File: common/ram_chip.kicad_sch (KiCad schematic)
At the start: 3 parts, among them U8 71016S12PHG8

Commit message: Memory Controller- Initial setup
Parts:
- renumbered C9 to C17, C10 to C18, U8 to U14

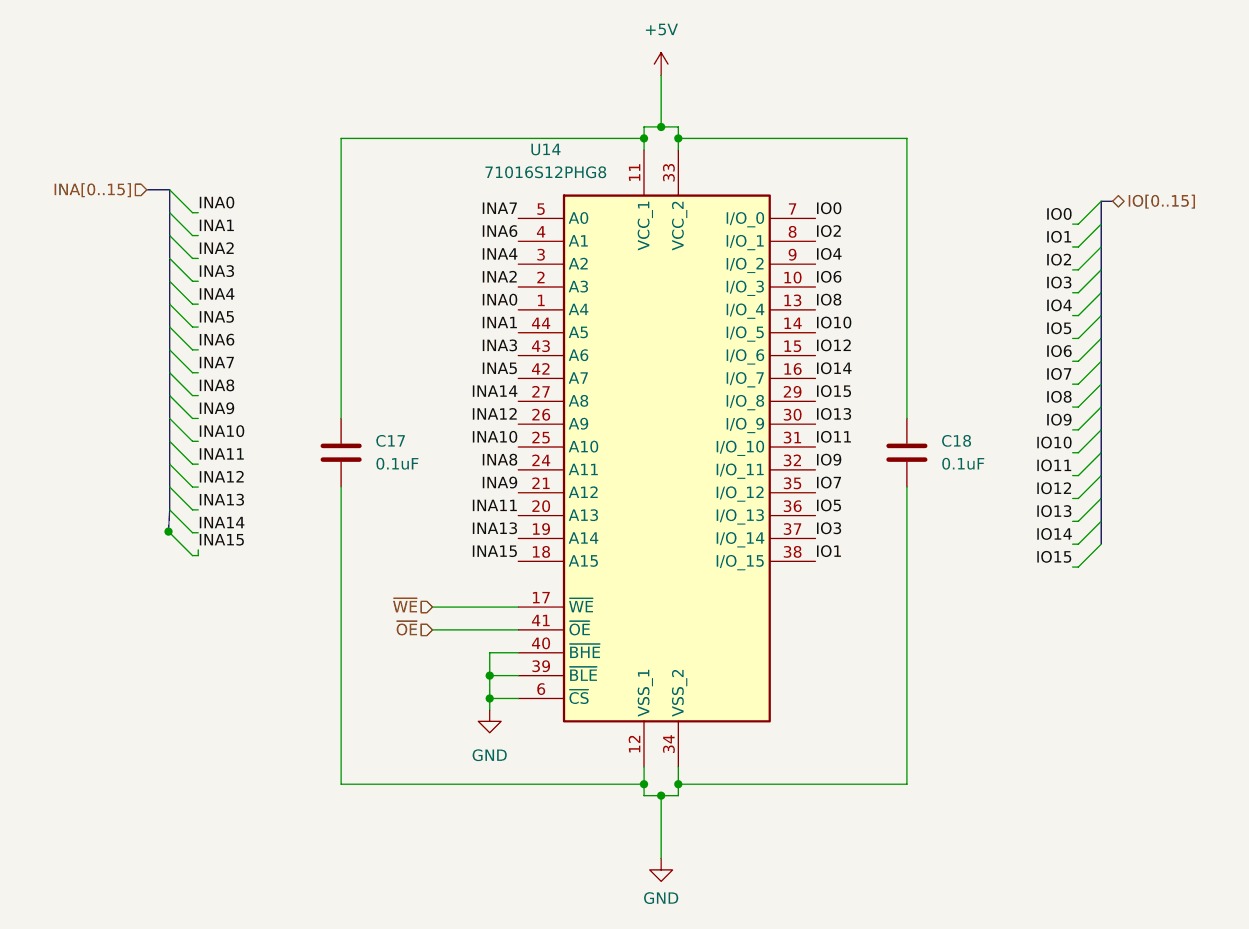
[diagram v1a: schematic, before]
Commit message: Memory Controller fabrication checks complete
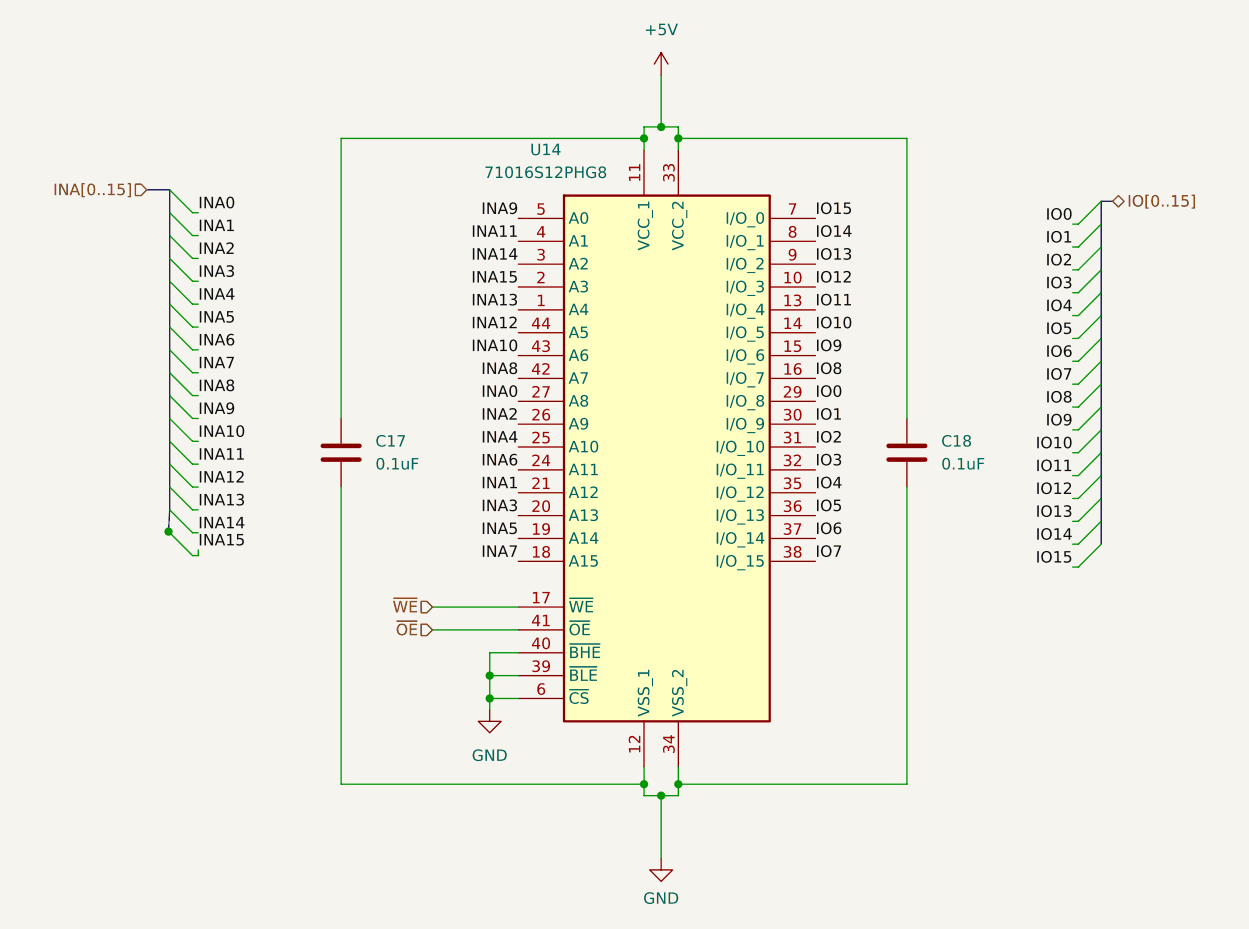
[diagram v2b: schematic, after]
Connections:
- net INA0: now also U14.27 (A8); no longer U14.1 (A4)
- net INA1: now also U14.21 (A12); no longer U14.44 (A5)
- net INA10: now also U14.43 (A6); no longer U14.25 (A10)
- net INA11: now also U14.4 (A1); no longer U14.20 (A13)
- net INA12: now also U14.44 (A5); no longer U14.26 (A9)
- net INA13: now also U14.1 (A4); no longer U14.19 (A14)
- net INA14: now also U14.3 (A2); no longer U14.27 (A8)
- net INA15: now also U14.2 (A3); no longer U14.18 (A15)
- net INA2: now also U14.26 (A9); no longer U14.2 (A3)
- net INA3: now also U14.20 (A13); no longer U14.43 (A6)
- net INA4: now also U14.25 (A10); no longer U14.3 (A2)
- net INA5: now also U14.19 (A14); no longer U14.42 (A7)
- net INA6: now also U14.24 (A11); no longer U14.4 (A1)
- net INA7: now also U14.18 (A15); no longer U14.5 (A0)
- net INA8: now also U14.42 (A7); no longer U14.24 (A11)
- net INA9: now also U14.5 (A0); no longer U14.21 (A12)
- net IO0: now also U14.29 (I/O_8); no longer U14.7 (I/O_0)
- net IO1: now also U14.30 (I/O_9); no longer U14.38 (I/O_15)
- net IO11: now also U14.13 (I/O_4); no longer U14.31 (I/O_10)
- net IO12: now also U14.10 (I/O_3); no longer U14.15 (I/O_6)
- net IO13: now also U14.9 (I/O_2); no longer U14.30 (I/O_9)
- net IO14: now also U14.8 (I/O_1); no longer U14.16 (I/O_7)
- net IO15: now also U14.7 (I/O_0); no longer U14.29 (I/O_8)
- net IO2: now also U14.31 (I/O_10); no longer U14.8 (I/O_1)
- net IO3: now also U14.32 (I/O_11); no longer U14.37 (I/O_14)
- net IO4: now also U14.35 (I/O_12); no longer U14.9 (I/O_2)
- net IO6: now also U14.37 (I/O_14); no longer U14.10 (I/O_3)
- net IO7: now also U14.38 (I/O_15); no longer U14.35 (I/O_12)
- net IO8: now also U14.16 (I/O_7); no longer U14.13 (I/O_4)
- net IO9: now also U14.15 (I/O_6); no longer U14.32 (I/O_11)
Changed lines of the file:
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@@
 		)
 	)
-	(label "INA9"
+	(label "INA1"
 		(at 100.33 91.44 180)
 		(effects
@@
 		)
 	)
+	(label "INA7"
+		(at 100.33 99.06 180)
+		(effects
+			(font
+				(size 1.27 1.27)
+			)
+			(justify right bottom)
+		)
+	)
 	(label "INA15"
-		(at 100.33 99.06 180)
-		(effects
-			(font
-				(size 1.27 1.27)
-			)
-			(justify right bottom)
-		)
-	)
-	(label "INA2"
 		(at 100.33 68.58 180)
 		(effects
@@
 		)
 	)
-	(label "INA12"
+	(label "INA2"
 		(at 100.33 83.82 180)
 		(effects
@@
 		)
 	)
-	(label "INA8"
+	(label "INA6"
 		(at 100.33 88.9 180)
 		(effects
@@
 		)
 	)
-	(label "INA10"
+	(label "INA4"
 		(at 100.33 86.36 180)
 		(effects
@@
 		)
 	)
-	(label "INA7"
+	(label "INA9"
 		(at 100.33 60.96 180)
 		(effects
@@
 		)
 	)
-	(label "INA3"
+	(label "INA10"
 		(at 100.33 76.2 180)
 		(effects
@@
 		)
 	)
+	(label "INA0"
+		(at 100.33 81.28 180)
+		(effects
+			(font
+				(size 1.27 1.27)
+			)
+			(justify right bottom)
+		)
+	)
 	(label "INA14"
-		(at 100.33 81.28 180)
-		(effects
-			(font
-				(size 1.27 1.27)
-			)
-			(justify right bottom)
-		)
-	)
-	(label "INA4"
 		(at 100.33 66.04 180)
 		(effects
@@
 		)
 	)
-	(label "INA13"
+	(label "INA5"
 		(at 100.33 96.52 180)
 		(effects
@@
 		)
 	)
-	(label "IO7"
+	(label "IO4"
 		(at 133.35 91.44 0)
 		(effects
@@
 		)
 	)
-	(label "IO9"
+	(label "IO3"
 		(at 133.35 88.9 0)
 		(effects
@@
 		)
 	)
-	(label "IO3"
+	(label "IO6"
 		(at 133.35 96.52 0)
 		(effects
@@
 		)
 	)
-	(label "INA6"
+	(label "INA11"
 		(at 100.33 63.5 180)
 		(effects
@@
 		)
 	)
-	(label "IO2"
+	(label "IO14"
 		(at 133.35 63.5 0)
 		(effects
@@
 		)
 	)
-	(label "INA0"
+	(label "INA13"
 		(at 100.33 71.12 180)
 		(effects
@@
 		)
 	)
-	(label "IO1"
+	(label "IO7"
 		(at 133.35 99.06 0)
 		(effects
@@
 		)
 	)
-	(label "IO4"
+	(label "IO13"
 		(at 133.35 66.04 0)
 		(effects
@@
 		)
 	)
-	(label "INA1"
+	(label "INA12"
 		(at 100.33 73.66 180)
 		(effects
@@
 		)
 	)
-	(label "IO11"
+	(label "IO2"
 		(at 133.35 86.36 0)
 		(effects
@@
 		)
 	)
-	(label "INA5"
+	(label "INA8"
 		(at 100.33 78.74 180)
 		(effects
@@
 		)
 	)
-	(label "IO6"
+	(label "IO12"
 		(at 133.35 68.58 0)
 		(effects
@@
 		)
 	)
-	(label "IO0"
+	(label "IO15"
 		(at 133.35 60.96 0)
 		(effects
@@
 		)
 	)
-	(label "INA11"
+	(label "INA3"
 		(at 100.33 93.98 180)
 		(effects
@@
 		)
 	)
-	(label "IO15"
+	(label "IO0"
 		(at 133.35 81.28 0)
 		(effects
@@
 		)
 	)
-	(label "IO12"
+	(label "IO9"
 		(at 133.35 76.2 0)
 		(effects
@@
 		)
 	)
-	(label "IO13"
+	(label "IO1"
 		(at 133.35 83.82 0)
 		(effects
@@
 		)
 	)
-	(label "IO14"
+	(label "IO8"
 		(at 133.35 78.74 0)
 		(effects
@@
 		)
 	)
-	(label "IO8"
+	(label "IO11"
 		(at 133.35 71.12 0)
 		(effects
@@
 		(dnp no)
 		(fields_autoplaced yes)
-		(property "Reference" "#PWR036"
+		(property "Reference" "#PWR0106"
 			(at 116.205 138.43 0)
 			(effects
@@
 				)
 			)
-			(project "AOS16 Double Buffer"
+			(project "Memory Controller"
 				(path "/a2e955d2-87ce-495b-9d0c-0c0d88eefe1c/7d522591-beb1-4e23-8710-d54fb933ebb3"
-					(reference "#PWR036")
+					(reference "#PWR0106")
 					(unit 1)
 				)
@@
 				)
 			)
-			(project "AOS16 Double Buffer"
+			(project "Memory Controller"
 				(path "/a2e955d2-87ce-495b-9d0c-0c0d88eefe1c/7d522591-beb1-4e23-8710-d54fb933ebb3"
 					(reference "C17")
@@
 		(dnp no)
 		(fields_autoplaced yes)
-		(property "Reference" "#PWR035"
+		(property "Reference" "#PWR0108"
 			(at 116.205 48.895 0)
 			(effects
@@
 				)
 			)
-			(project "AOS16 Double Buffer"
+			(project "Memory Controller"
 				(path "/a2e955d2-87ce-495b-9d0c-0c0d88eefe1c/7d522591-beb1-4e23-8710-d54fb933ebb3"
-					(reference "#PWR035")
+					(reference "#PWR0108")
 					(unit 1)
 				)
@@
 				)
 			)
-			(project "AOS16 Double Buffer"
+			(project "Memory Controller"
 				(path "/a2e955d2-87ce-495b-9d0c-0c0d88eefe1c/7d522591-beb1-4e23-8710-d54fb933ebb3"
 					(reference "U14")
@@
 		(dnp no)
 		(fields_autoplaced yes)
-		(property "Reference" "#PWR034"
+		(property "Reference" "#PWR0107"
 			(at 97.155 121.92 0)
 			(effects
@@
 				)
 			)
-			(project "AOS16 Double Buffer"
+			(project "Memory Controller"
 				(path "/a2e955d2-87ce-495b-9d0c-0c0d88eefe1c/7d522591-beb1-4e23-8710-d54fb933ebb3"
-					(reference "#PWR034")
+					(reference "#PWR0107")
 					(unit 1)
 				)
@@
 				)
 			)
-			(project "AOS16 Double Buffer"
+			(project "Memory Controller"
 				(path "/a2e955d2-87ce-495b-9d0c-0c0d88eefe1c/7d522591-beb1-4e23-8710-d54fb933ebb3"
 					(reference "C18")
